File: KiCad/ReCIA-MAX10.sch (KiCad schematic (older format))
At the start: 6 parts, among them U1 AMS1117-3.3, U2 10M02SCU169, U5 8520_DIP

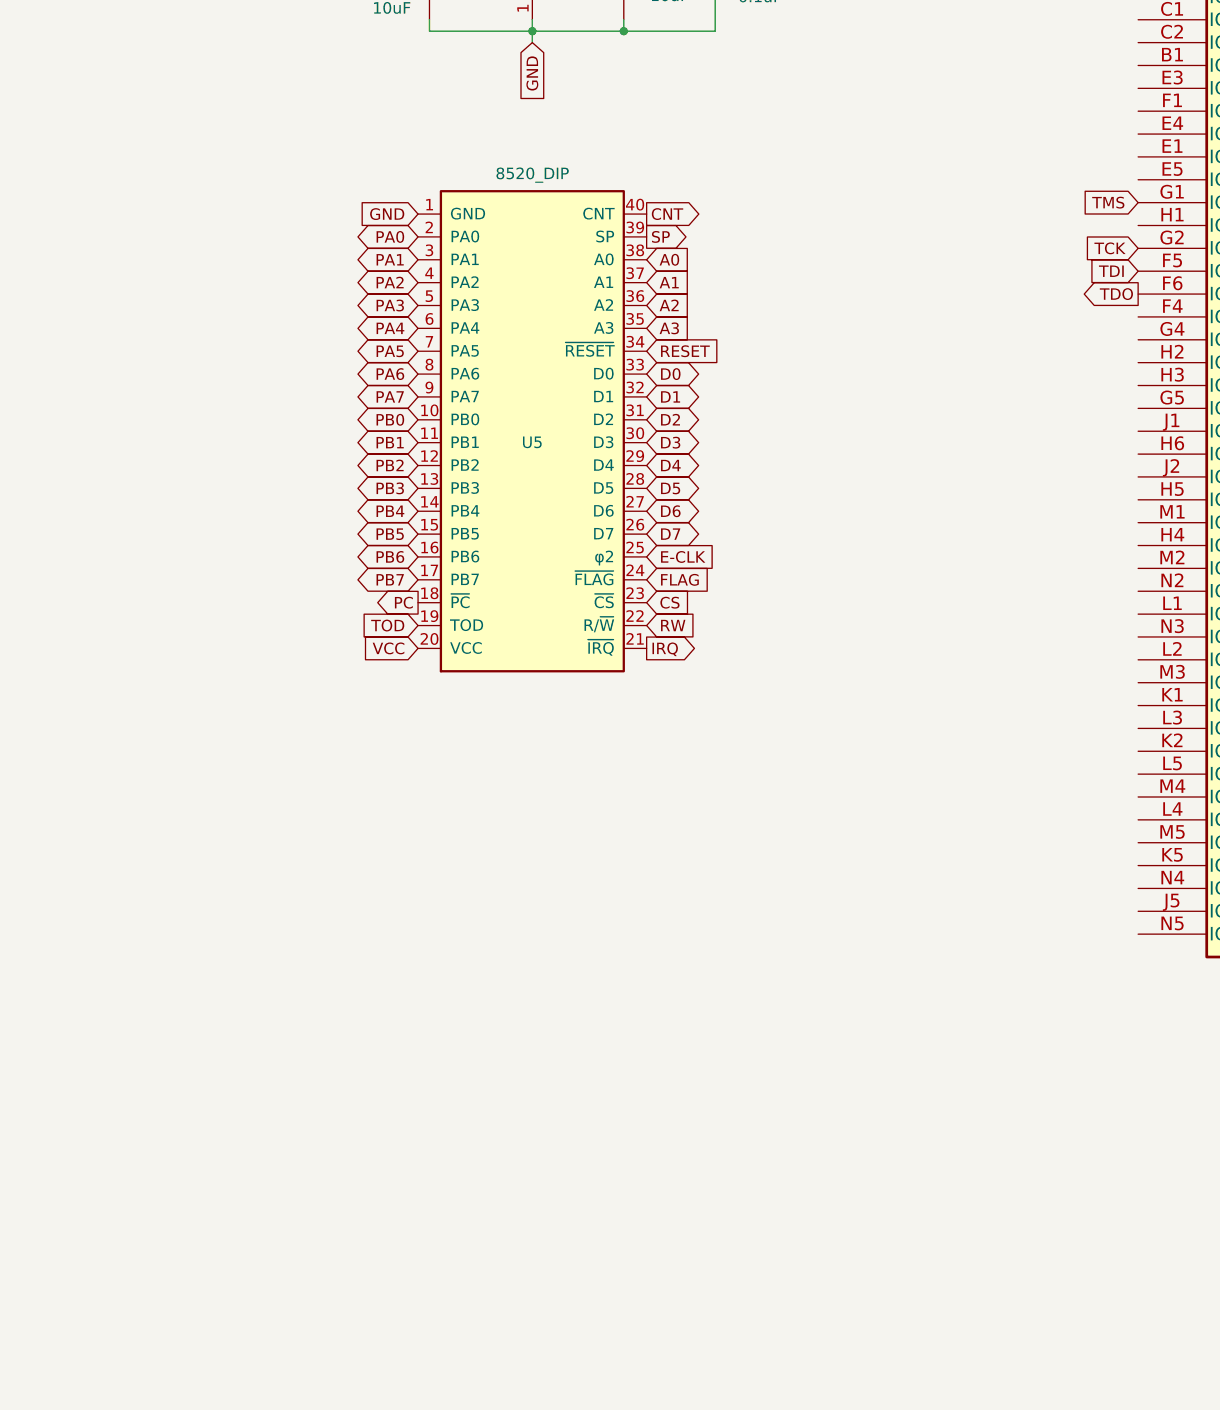
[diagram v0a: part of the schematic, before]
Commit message: Add FET bus-switch level shifters SN74CBT16210
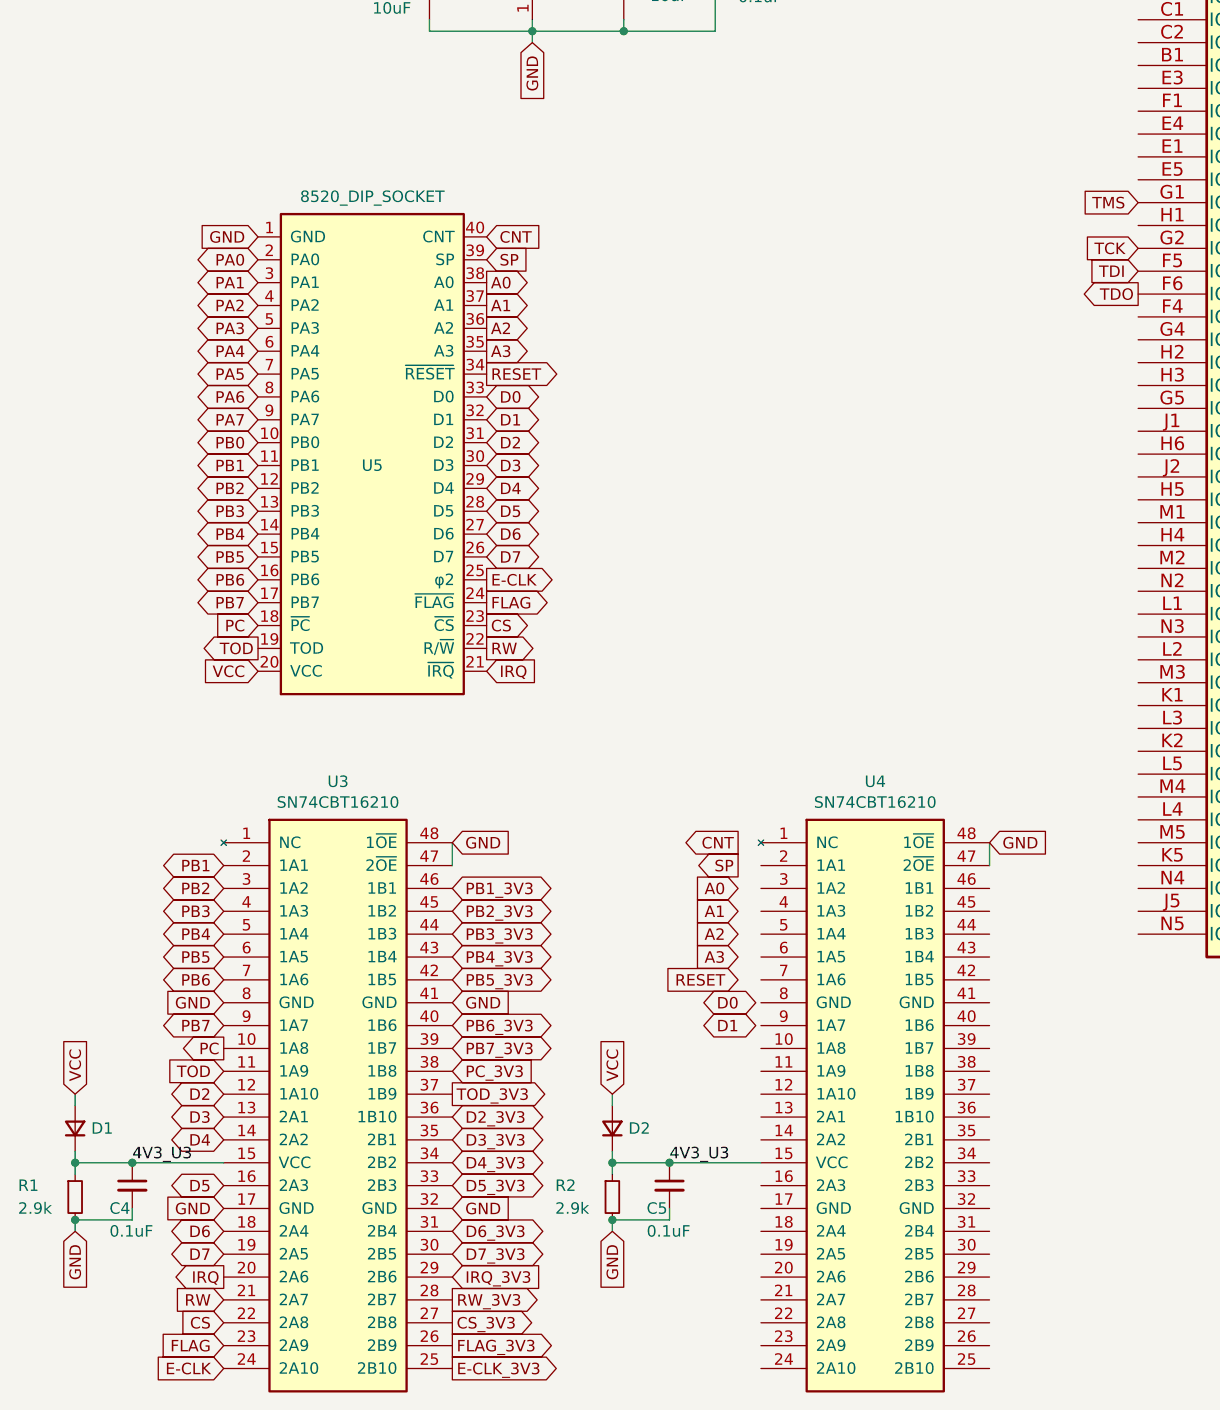
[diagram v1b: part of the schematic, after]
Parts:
- added C4, C5: 0.1uF, Capacitor_SMD:C_0603_1608Metric_Pad1.08x0.95mm_HandSolder, symbol Device:C_Small
- added D1, D2: D_Small, Diode_SMD:D_0603_1608Metric_Pad1.05x0.95mm_HandSolder, symbol Device:D_Small
- added R1, R2: 2.9k, Capacitor_SMD:C_0603_1608Metric_Pad1.08x0.95mm_HandSolder, symbol Device:R_Small
- added U3, U4: SN74CBT16210, Package_SO:TSSOP-48_4.4x9.7mm_P0.4mm, symbol ReCIA:SN74CBT16210
- U5: value 8520_DIP -> 8520_DIP_SOCKET
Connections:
- net CS: now also U3.22 (2A8)
- net D2: now also U3.12 (1A10)
- net D3: now also U3.13 (2A1)
- net D4: now also U3.14 (2A2)
- net D5: now also U3.16 (2A3)
- net D6: now also U3.18 (2A4)
- net D7: now also U3.19 (2A5)
- net E-CLK: now also U3.24 (2A10)
- net FLAG: now also U3.23 (2A9)
- net GND: now also C4.2, C5.2, R1.2, R2.2, U3.17 (GND), U3.32 (GND), U3.41 (GND), U3.47 (2~OE), U3.48 (1~OE), U3.8 (GND), U4.47 (2~OE), U4.48 (1~OE)
- net IRQ: now also U3.20 (2A6)
- net PB1: now also U3.2 (1A1)
- net PB2: now also U3.3 (1A2)
- net PB3: now also U3.4 (1A3)
- net PB4: now also U3.5 (1A4)
- net PB5: now also U3.6 (1A5)
- net PB6: now also U3.7 (1A6)
- net PB7: now also U3.9 (1A7)
- net PC: now also U3.10 (1A8)
- net RW: now also U3.21 (2A7)
- net TOD: now also U3.11 (1A9)
- net VCC: now also D1.2 (A), D2.2 (A)
- new net 4V3_U3: C4.1, C5.1, D1.1 (K), D2.1 (K), R1.1, R2.1, U3.15 (VCC), U4.15 (VCC)
- new net CS_3V3: U3.27 (2B8)
- new net D2_3V3: U3.36 (1B10)
- new net D3_3V3: U3.35 (2B1)
- new net D4_3V3: U3.34 (2B2)
- new net D5_3V3: U3.33 (2B3)
- new net D6_3V3: U3.31 (2B4)
- new net D7_3V3: U3.30 (2B5)
- new net E-CLK_3V3: U3.25 (2B10)
- new net FLAG_3V3: U3.26 (2B9)
- new net IRQ_3V3: U3.29 (2B6)
- new net PB1_3V3: U3.46 (1B1)
- new net PB2_3V3: U3.45 (1B2)
- new net PB3_3V3: U3.44 (1B3)
- new net PB4_3V3: U3.43 (1B4)
- new net PB5_3V3: U3.42 (1B5)
- new net PB6_3V3: U3.40 (1B6)
- new net PB7_3V3: U3.39 (1B7)
- new net PC_3V3: U3.38 (1B8)
- new net RW_3V3: U3.28 (2B7)
- new net TOD_3V3: U3.37 (1B9)
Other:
- moved on the sheet: U5

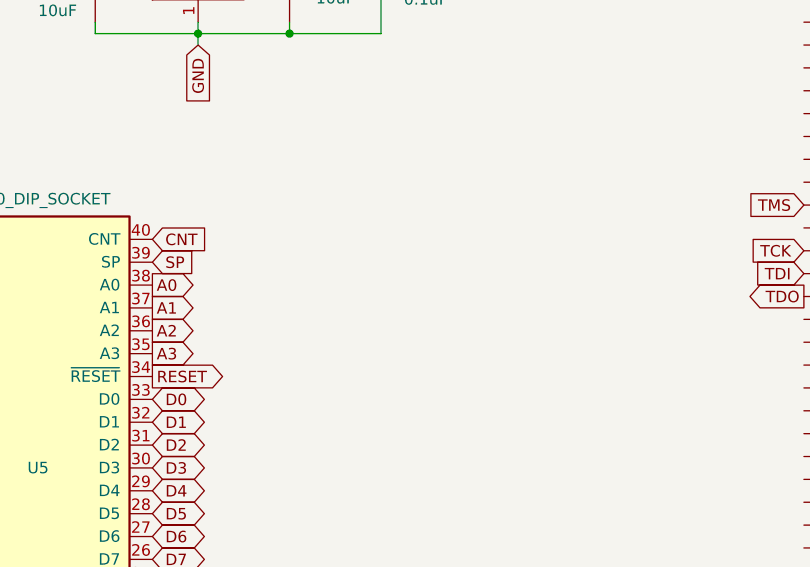
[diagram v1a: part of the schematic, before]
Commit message: Add JTAG-header
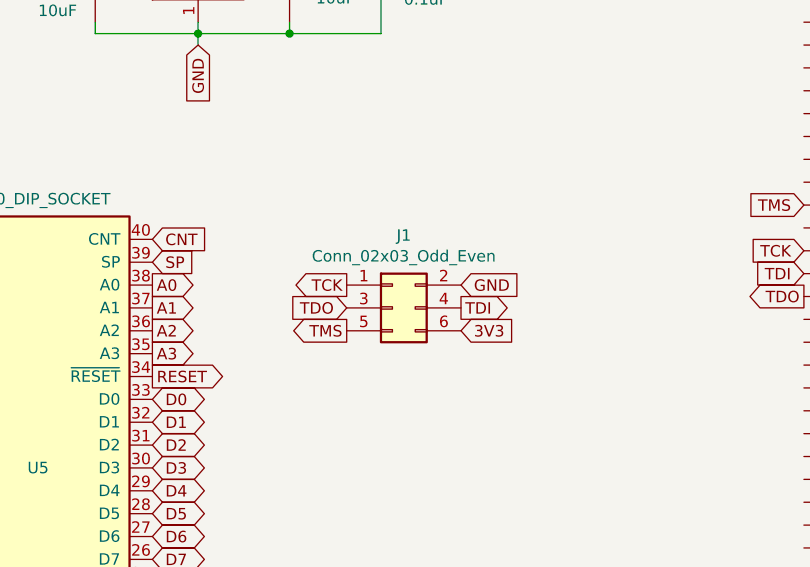
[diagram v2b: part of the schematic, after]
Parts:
- added J1: Conn_02x03_Odd_Even, Connector_PinHeader_2.00mm:PinHeader_2x03_P2.00mm_Vertical_SMD, symbol Connector_Generic:Conn_02x03_Odd_Even
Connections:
- net 3V3: now also J1.6 (Pin_6)
- net GND: now also J1.2 (Pin_2)
- net TCK: now also J1.1 (Pin_1)
- net TDI: now also J1.4 (Pin_4)
- net TDO: now also J1.3 (Pin_3)
- net TMS: now also J1.5 (Pin_5)
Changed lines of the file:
@@
 Text Label 3350 6550 0    50   ~ 0
 4V3_U3
+$Comp
+L Connector_Generic:Conn_02x03_Odd_Even J1
+U 1 1 66E424CD
+P 3600 2800
+F 0 "J1" H 3650 3117 50  0000 C CNN
+F 1 "Conn_02x03_Odd_Even" H 3650 3026 50  0000 C CNN
+F 2 "Connector_PinHeader_2.00mm:PinHeader_2x03_P2.00mm_Vertical_SMD" H 3600 2800 50  0001 C CNN
+F 3 "~" H 3600 2800 50  0001 C CNN
+	1    3600 2800
+	1    0    0    -1
+$EndComp
+Text GLabel 3400 2700 0    50   Output ~ 0
+TCK
+Text GLabel 3400 2800 0    50   Input ~ 0
+TDO
+Text GLabel 3400 2900 0    50   Output ~ 0
+TMS
+Text GLabel 3900 2800 2    50   Output ~ 0
+TDI
+Text GLabel 3900 2700 2    50   Input ~ 0
+GND
+Text GLabel 3900 2900 2    50   Input ~ 0
+3V3
 $EndSCHEMATC
